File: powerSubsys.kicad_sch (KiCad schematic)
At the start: 36 parts, among them J1 Conn_02x16_Odd_Even, J2 JST_PH_2mm, Q1 PN2222A, U1 INA219AxD, U2 DRV8244HQRYJRQ1, U3 BQ24074RGT, U4 TPS22810DRV, U5 TPS22810DRV, U6 CH224K

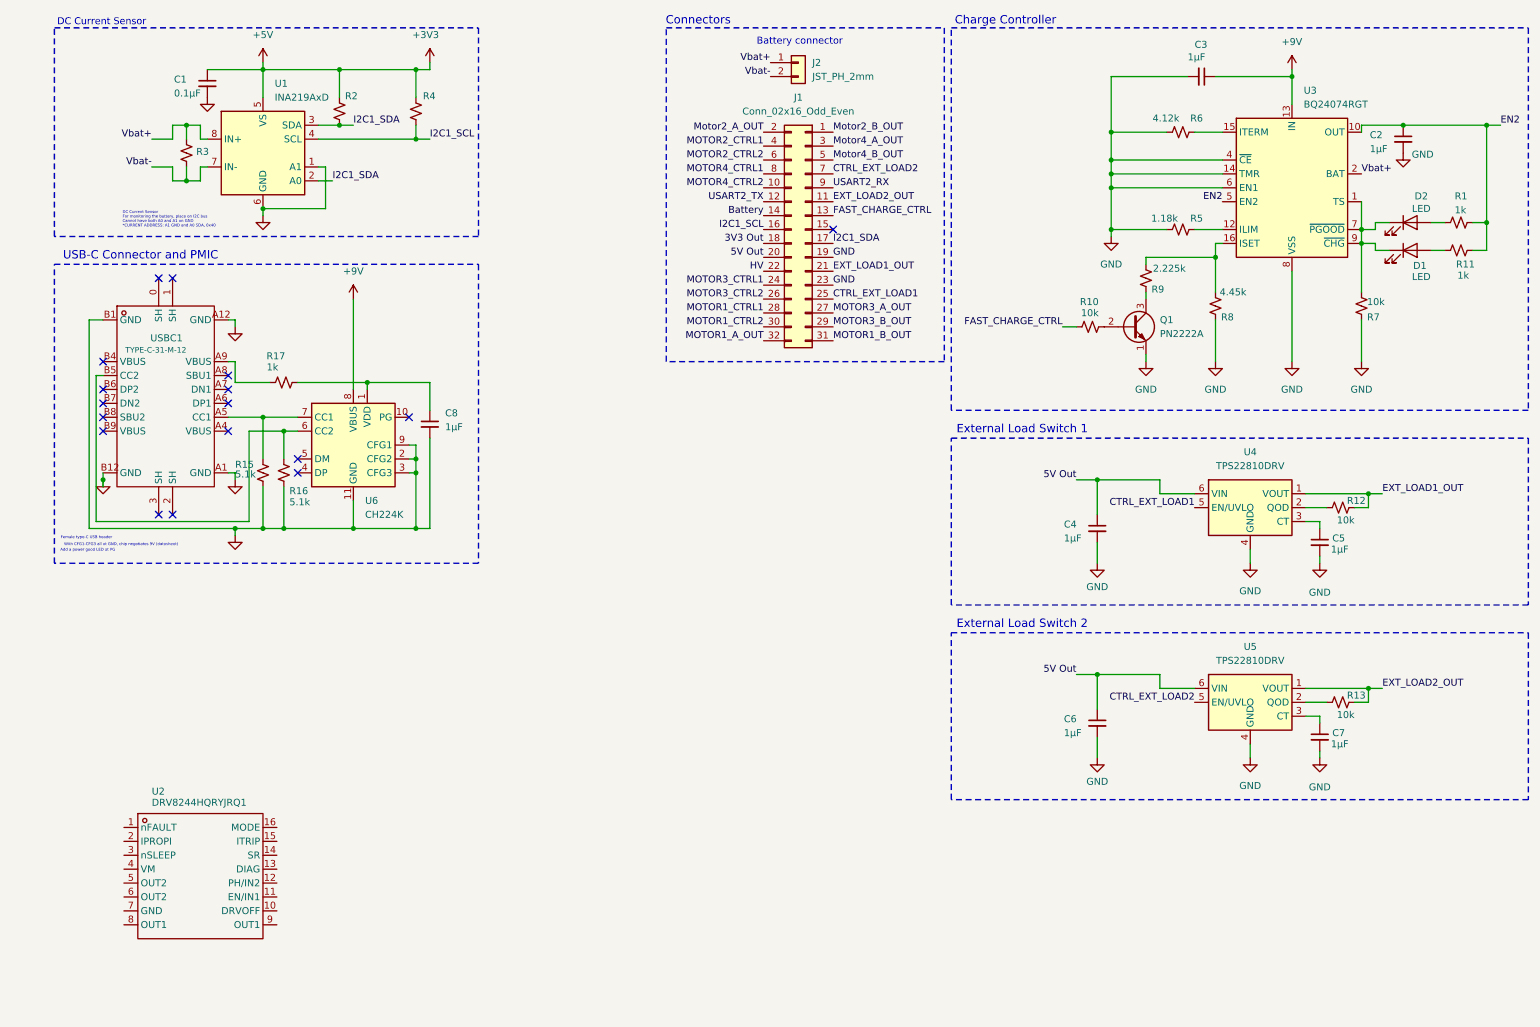
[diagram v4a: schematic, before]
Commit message: Added motor drivers
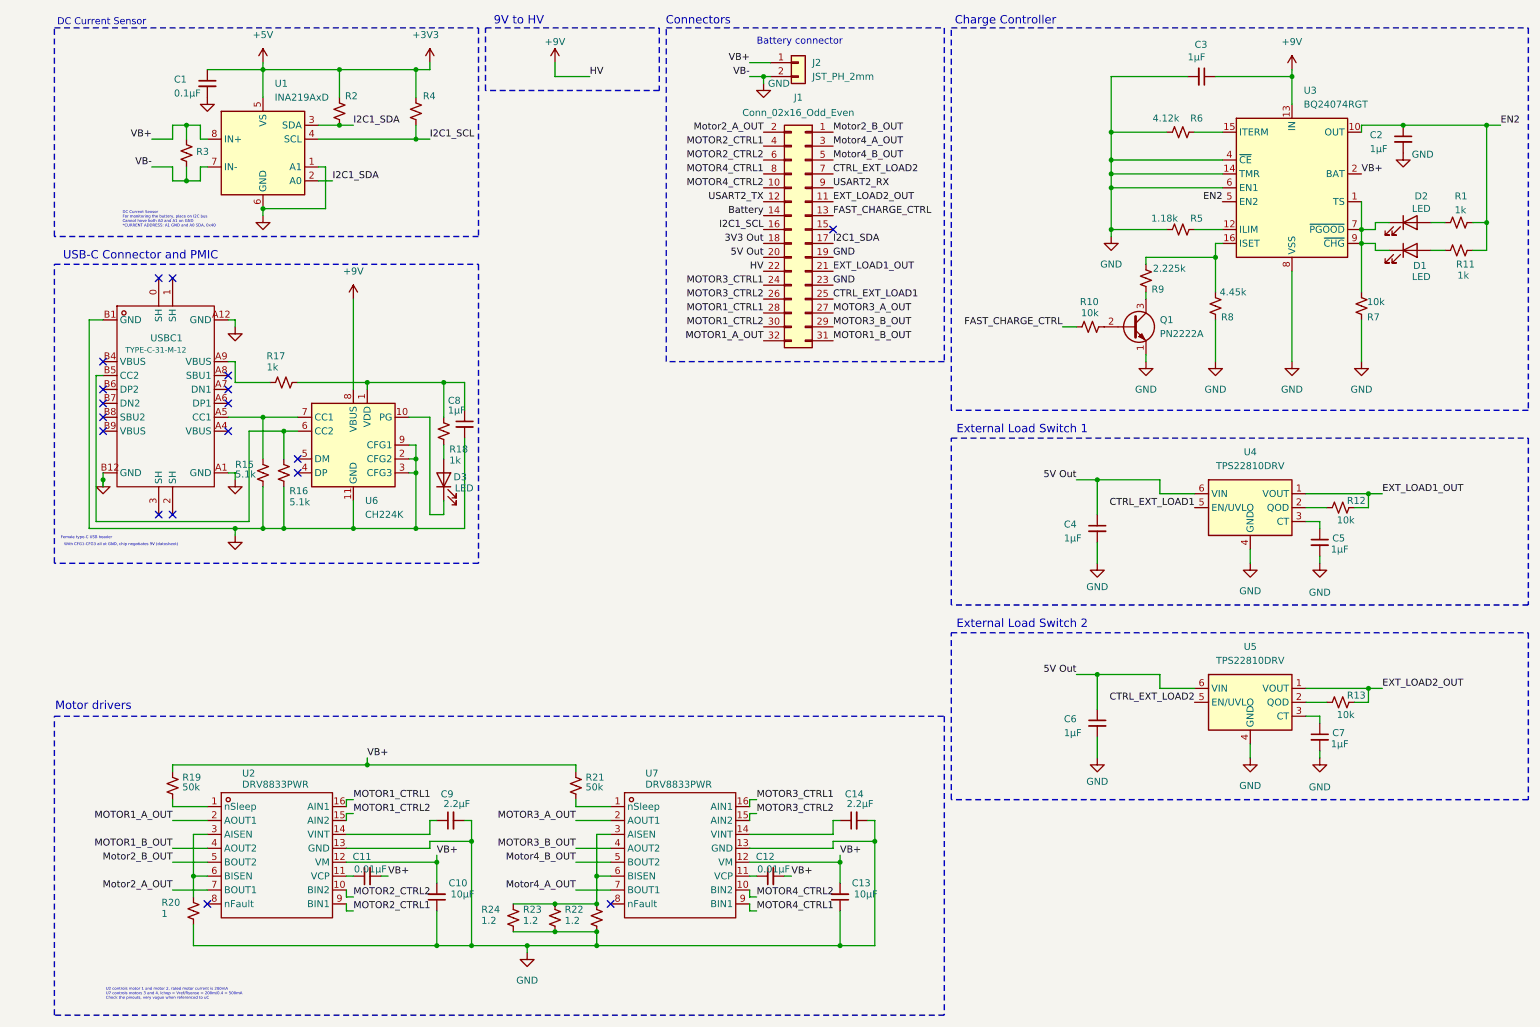
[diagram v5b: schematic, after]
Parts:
- removed U2: DRV8244HQRYJRQ1, VQFN-16_L6.0-W3.0-P0.50-TL, symbol DRV8244HQRYJRQ11_DRV8244HQRYJRQ1-altium-import:root_0_DRV8244HQRYJRQ1_
- added C10, C13: 10μF, symbol Device:C_Small
- added C11, C12: 0.01μF, symbol Device:C_Small
- added C14, C9: 2.2μF, symbol Device:C_Small
- added D3: LED, symbol Device:LED
- added R18: 1k, symbol Device:R_Small_US
- added R19, R21: 50k, symbol Device:R_Small_US
- added R20: 1, symbol Device:R_Small_US
- added R22, R23, R24: 1.2, symbol Device:R_Small_US
- added U2, U7: DRV8833PWR, TSSOP-16_L5.0-W4.4-P0.65-LS6.4-BL, symbol hbridge-altium-import:root_0_DRV8833PWR_
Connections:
- net HV is gone; now on net +9V: J1.22 (Pin_22)
- net Vbat- is gone; now on net GND: J2.2 (Pin_2), R3.2, U1.7 (IN-)
- net GND: now also C10.1, C13.1, C14.2, C9.2, R20.2, R22.2, R23.2, R24.2, U2.13 (GND), U7.13 (GND)
- net MOTOR1_A_OUT: now also U2.2 (AOUT1)
- net MOTOR1_B_OUT: now also U2.4 (AOUT2)
- net MOTOR1_CTRL1: now also U2.16 (AIN1)
- net MOTOR1_CTRL2: now also U2.15 (AIN2)
- net MOTOR2_CTRL1: now also U2.9 (BIN1)
- net MOTOR2_CTRL2: now also U2.10 (BIN2)
- net MOTOR3_A_OUT: now also U7.2 (AOUT1)
- net MOTOR3_B_OUT: now also U7.4 (AOUT2)
- net MOTOR3_CTRL1: now also U7.16 (AIN1)
- net MOTOR3_CTRL2: now also U7.15 (AIN2)
- net MOTOR4_CTRL1: now also U7.9 (BIN1)
- net MOTOR4_CTRL2: now also U7.10 (BIN2)
- net Motor2_A_OUT: now also U2.7 (BOUT1)
- net Motor2_B_OUT: now also U2.5 (BOUT2)
- net Motor4_A_OUT: now also U7.7 (BOUT1)
- net Motor4_B_OUT: now also U7.5 (BOUT2)
- net at C8.1, R17.2, U6.1 (VDD): now also R18.1
- net at U6.10 (PG): now also D3.1 (K)
- net Vbat+ renamed VB+
- net VB+: now also C10.2, C11.2, C12.2, C13.2, R19.1, R21.1, U2.12 (VM), U7.12 (VM)
- new net: C9.1, U2.14 (VINT)
- new net: R21.2, U7.1 (nSleep)
- new net: R22.1, R23.1, R24.1, U7.3 (AISEN), U7.6 (BISEN)
- new net: C12.1, U7.11 (VCP)
- new net: C14.1, U7.14 (VINT)
- new net: R20.1, U2.3 (AISEN), U2.6 (BISEN)
- new net: C11.1, U2.11 (VCP)
- new net: R19.2, U2.1 (nSleep)
- new net: D3.2 (A), R18.2
- no-connect marks 17 -> 18
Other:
- note added: "9V to HV"
- note added: "Motor drivers"
- note added: "U2 controls motor 1 and motor 2, rated motor current is 200mA U7 controls motors 3 and 4, Ichop = Vref/Rsense = 200m/0.4 = 500mA Check the pinouts, very vague when referenced to uC"
- note removed: "Add a power good LED at PG"
- moved on the sheet: C8
